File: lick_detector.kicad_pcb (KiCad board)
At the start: 2 copper layers, 74.9 x 80.6 mm, 105 parts, among them P1 PWR_JACK_2.1x5.5_SMD_RA, SW1 SPDT_SLIDE_500A_SM, U1 DRV103, U2 DRV103, U3 DRV103, U4 DRV103, U5 DRV103, U6 DRV103, U7 DRV103, U8 DRV103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

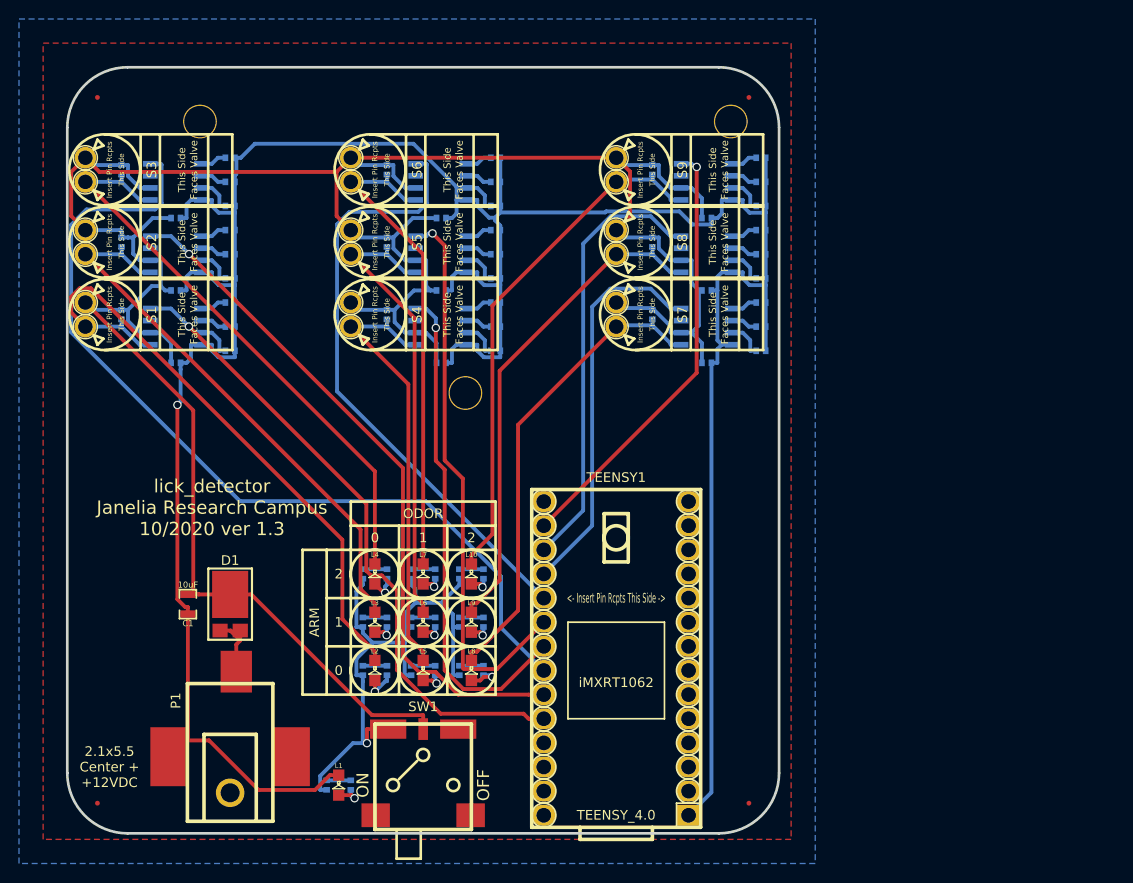
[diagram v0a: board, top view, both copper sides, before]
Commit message: Add ADXL313
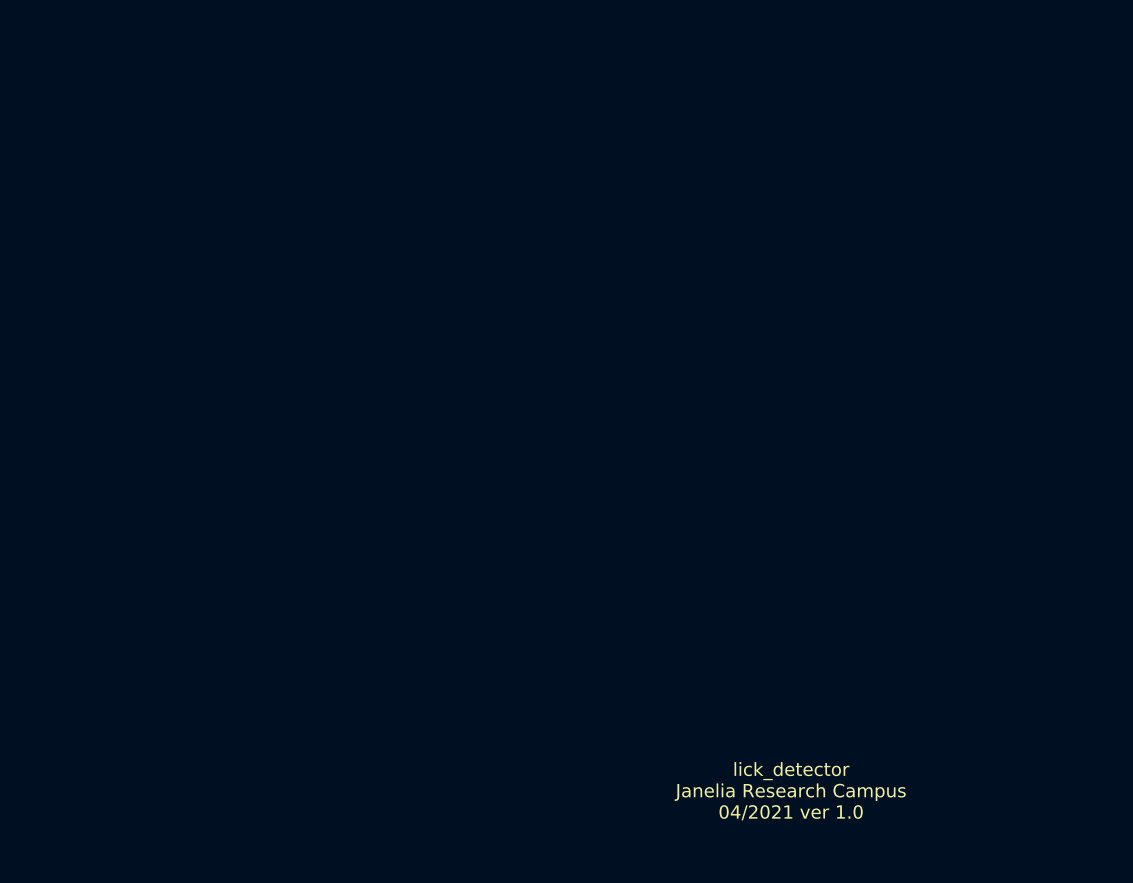
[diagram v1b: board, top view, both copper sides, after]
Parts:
- removed C1: 10uF, lick_detector:SM0805
- removed C10, C12, C14, C16, C18, C2, C4, C6, C8: 1uF, odor_spike_hold:SM0402_POL
- removed C11, C13, C15, C17, C19, C3, C5, C7, C9: 15nF, odor_spike_hold:SM0402
- removed D1: DIODE_SCHOTTKY_45V_10A, lick_detector:CFP15
- removed D10, D12, D14, D16, D18, D20, D4, D6, D8: DIODE_SCHOTTKY_0402, odor_spike_hold:SM0402_POL
- removed D11, D13, D15, D17, D19, D3, D5, D7, D9: DIODE_LOW_REV_CURRENT_0402, odor_spike_hold:SM0402_POL
- removed D2: DIODE_LOW_REV_CURRENT_0402, lick_detector:SM0402_POL
- removed FID1, FID2, FID3, FID4: FIDUCIAL, lick_detector:FIDUCIAL
- removed L1: LED_GRN, lick_detector:LED0805
- removed L10, L2, L3, L4, L5, L6, L7, L8, L9: LED_GRN, odor_spike_hold:LED0805
- removed MH1, MH2, MH3: VAL**, lick_detector:MOUNTING_HOLE_4-40
- removed P1: PWR_JACK_2.1x5.5_SMD_RA, lick_detector:DCJACK_3PAD_SMD_RA
- removed R1: 390, lick_detector:SM0402
- removed R10, R13, R16, R19, R22, R25, R28, R4, R7: 205k, odor_spike_hold:SM0402
- removed R11, R14, R17, R2, R20, R23, R26, R5, R8: 390, odor_spike_hold:SM0402
- removed R12, R15, R18, R21, R24, R27, R3, R6, R9: 150k, odor_spike_hold:SM0402
- removed S1, S2, S3, S4, S5, S6, S7, S8, S9: VAL**, odor_spike_hold:LEECO_LHDB
- removed SW1: SPDT_SLIDE_500A_SM, lick_detector:SPDT_SLIDE_500A_SM
- removed TEENSY1: TEENSY_4.0, lick_detector:TEENSY_4.0
- removed U1, U2, U3, U4, U5, U6, U7, U8, U9: DRV103, odor_spike_hold:SOIC_8
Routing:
- net GND: track 300.6 -> 0.00 mm, vias 1 -> 0
- net VCC: track 286.7 -> 0.00 mm
- net /ARM_0_ODOR_2: track 94.7 -> 0.00 mm
- net /ARM_0_ODOR_1: track 73.0 -> 0.00 mm, vias 1 -> 0
- net /ARM_0_ODOR_0: track 68.3 -> 0.00 mm, vias 1 -> 0
- net /odor_0/SH: track 66.2 -> 0.00 mm
- net /ARM_1_ODOR_2: track 64.0 -> 0.00 mm
- net /Vled: track 63.4 -> 0.00 mm, vias 1 -> 0
- net /odor_2/SH: track 61.2 -> 0.00 mm
- net /ARM_1_ODOR_1: track 59.6 -> 0.00 mm, vias 1 -> 0
- net /odor_1/SH: track 58.7 -> 0.00 mm
- net /odor_8/SH: track 55.0 -> 0.00 mm
- net /ARM_1_ODOR_0: track 53.1 -> 0.00 mm, vias 1 -> 0
- net /odor_7/SH: track 52.7 -> 0.00 mm
- net /odor_5/SH: track 51.8 -> 0.00 mm
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- removed copper zone on B.Cu, net GND
- removed copper zone on F.Cu, net VCC
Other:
- board outline removed
- board text added: "lick_detector Janelia Research Campus 04/2021 ver 1.0"
- board text removed: "0"
- board text removed: "1"
- board text removed: "2"
- board text removed: "2.1x5.5 Center + +12VDC"
- board text removed: "ARM"
- board text removed: "ARM 0"
- board text removed: "ARM 1"
- board text removed: "ARM 2"
- board text removed: "ODOR"
- board text removed: "ODOR 0"
- board text removed: "ODOR 1"
- board text removed: "ODOR 2"
- board text removed: "lick_detector Janelia Research Campus 10/2020 ver 1.3"

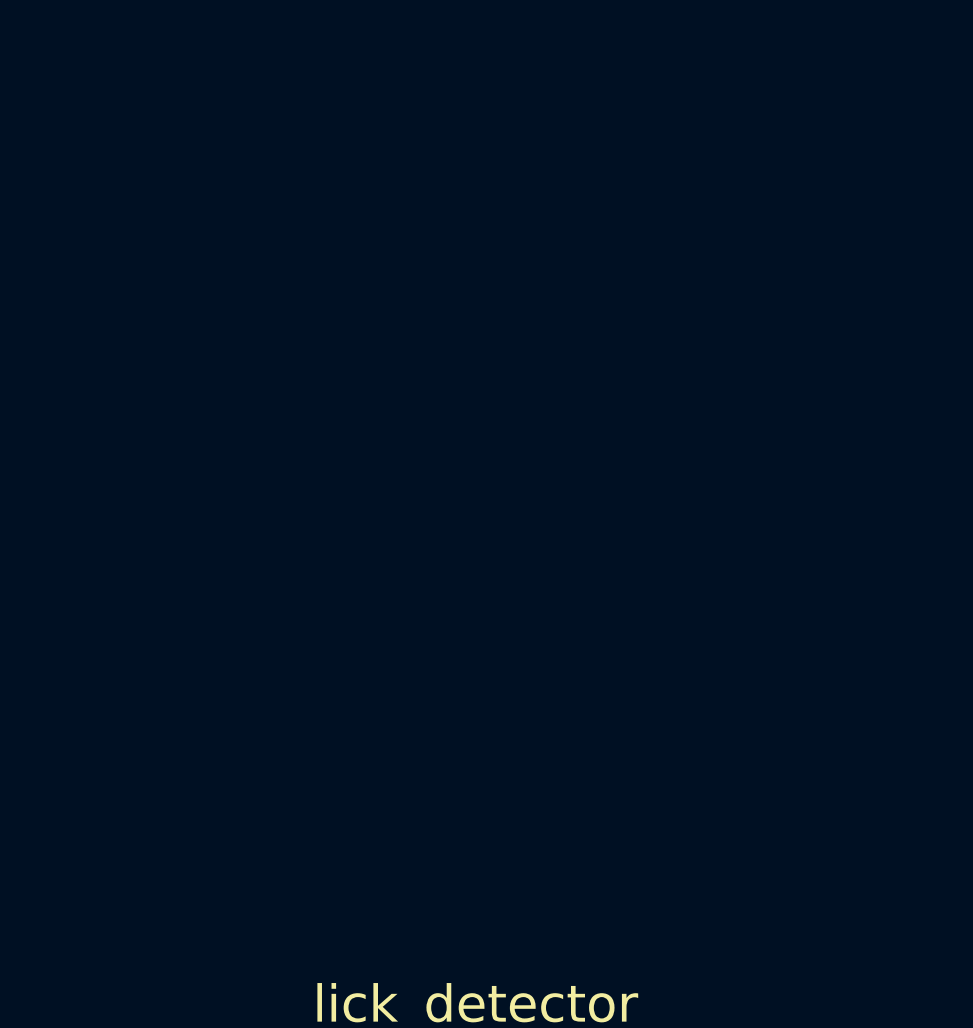
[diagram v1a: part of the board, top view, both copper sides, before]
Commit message: Add capacitors and receptacle
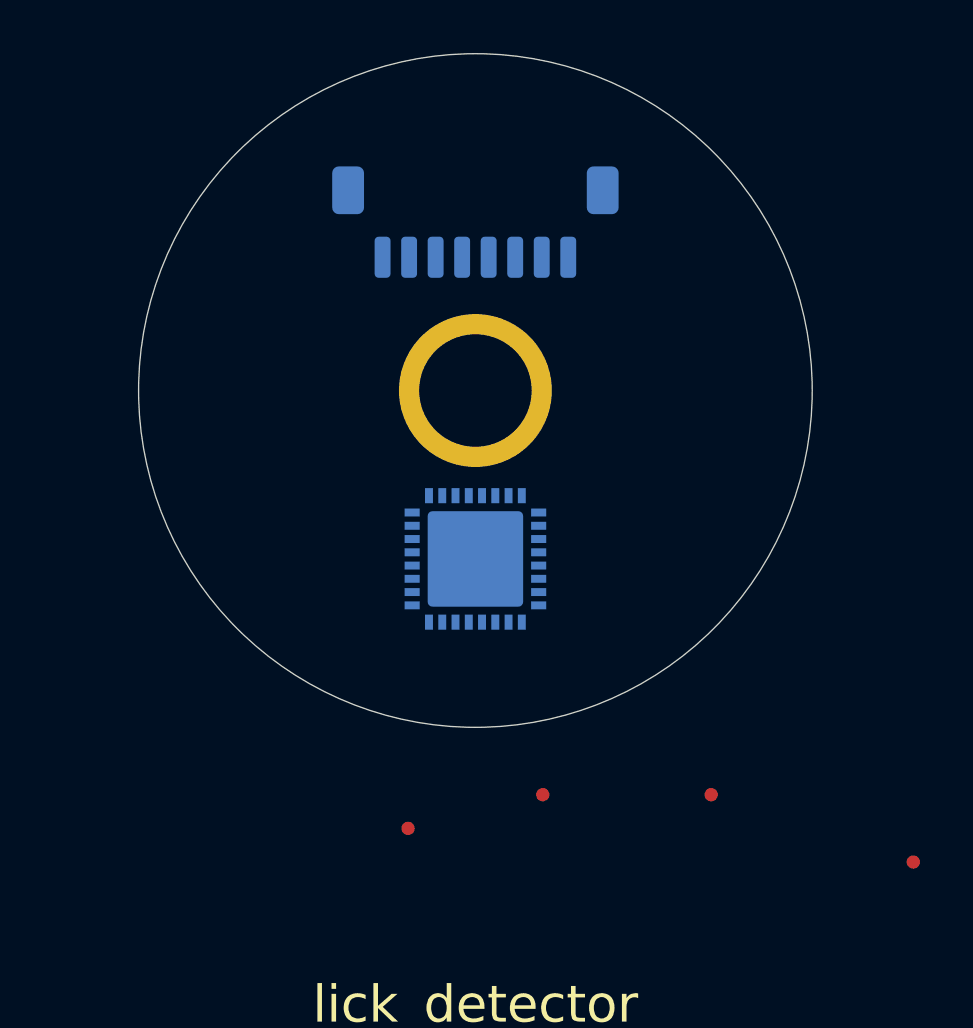
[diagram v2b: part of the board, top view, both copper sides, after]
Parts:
- added FID1: FIDUCIAL, lick_detector:FIDUCIAL, F.Cu at (129.5, 116.8)
- added FID2: FIDUCIAL, lick_detector:FIDUCIAL, F.Cu at (143.5, 119.4)
- added FID3: FIDUCIAL, lick_detector:FIDUCIAL, F.Cu at (135.9, 116.8)
- added FID4: FIDUCIAL, lick_detector:FIDUCIAL, F.Cu at (124.5, 118.1)
- added P1: CONN_PICO_CLASP_8, lick_detector:Molex_Pico-Clasp_501331-0807_1x08-1MP_P1.00mm_Vertical, B.Cu at (127.0, 95.2)
- added P2: RECEPTACLE_2MM, lick_detector:RECEPTACLE_2MM, B.Cu at (127.0, 101.6)
- added U1: ADXL313, lick_detector:LFCSP-32-1EP_5x5mm_P0.5mm_EP3.6x3.6mm, B.Cu at (127.0, 108.0)
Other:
- board outline added: 25.4 x 25.4 mm

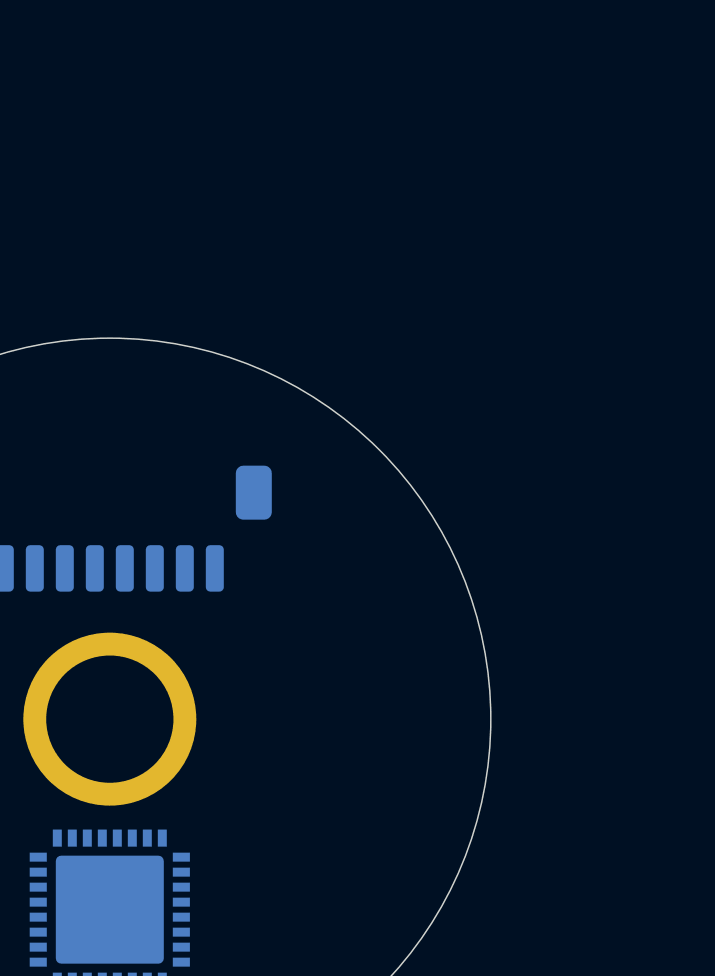
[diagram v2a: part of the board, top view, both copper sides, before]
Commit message: Add BUFFER_TRI_STATE and BUFFER_2_ELEMENT
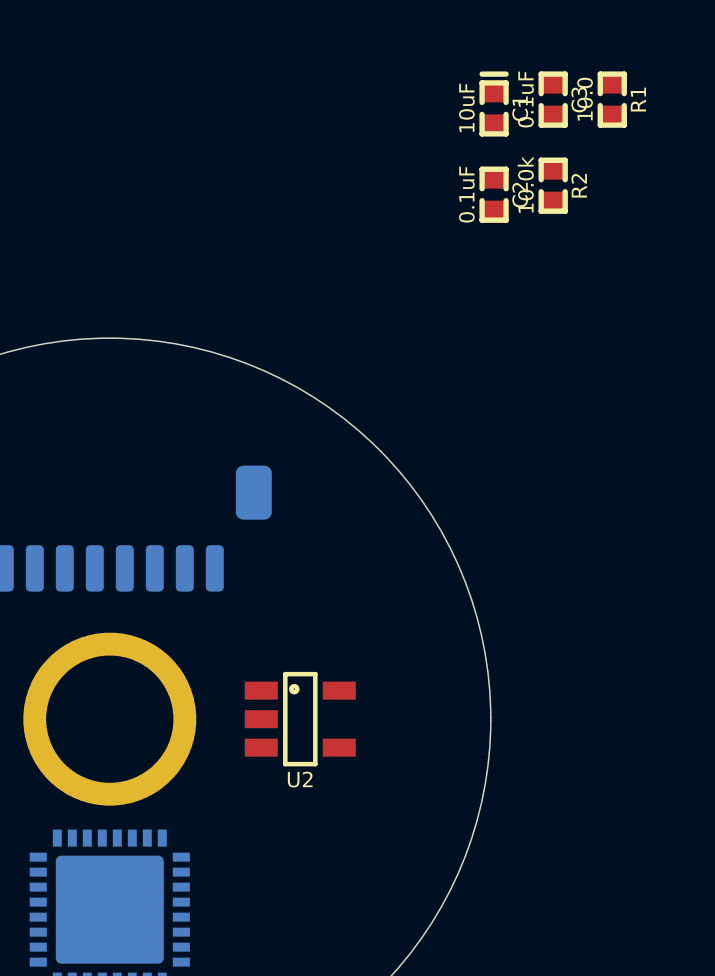
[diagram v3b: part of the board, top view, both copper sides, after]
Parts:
- added C1: 10uF, lick_detector:SM0402_POL, F.Cu at (139.8, 81.2)
- added C2: 0.1uF, lick_detector:SM0402, F.Cu at (139.8, 84.1)
- added C3: 0.1uF, lick_detector:SM0402, F.Cu at (141.8, 80.9)
- added R1: 10.0, lick_detector:SM0402, F.Cu at (143.7, 80.9)
- added R2: 10.0k, lick_detector:SM0402, F.Cu at (141.8, 83.8)
- added U2: BUFFER_TRI_STATE, lick_detector:SOT-23-5, F.Cu at (133.3, 101.6)
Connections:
- P1 pad 1: (no net) -> VAA
- P1 pad 8: (no net) -> GND
- U1 pad 1: (no net) -> GND
- U1 pad 23: (no net) -> /MISO_UB
- U1 pad 3: (no net) -> GND
- U1 pad 33: (no net) -> GND
- U1 pad 4: (no net) -> GND
- U1 pad 5: (no net) -> Net-(R1-Pad1)
- U1 pad 6: (no net) -> /~CS

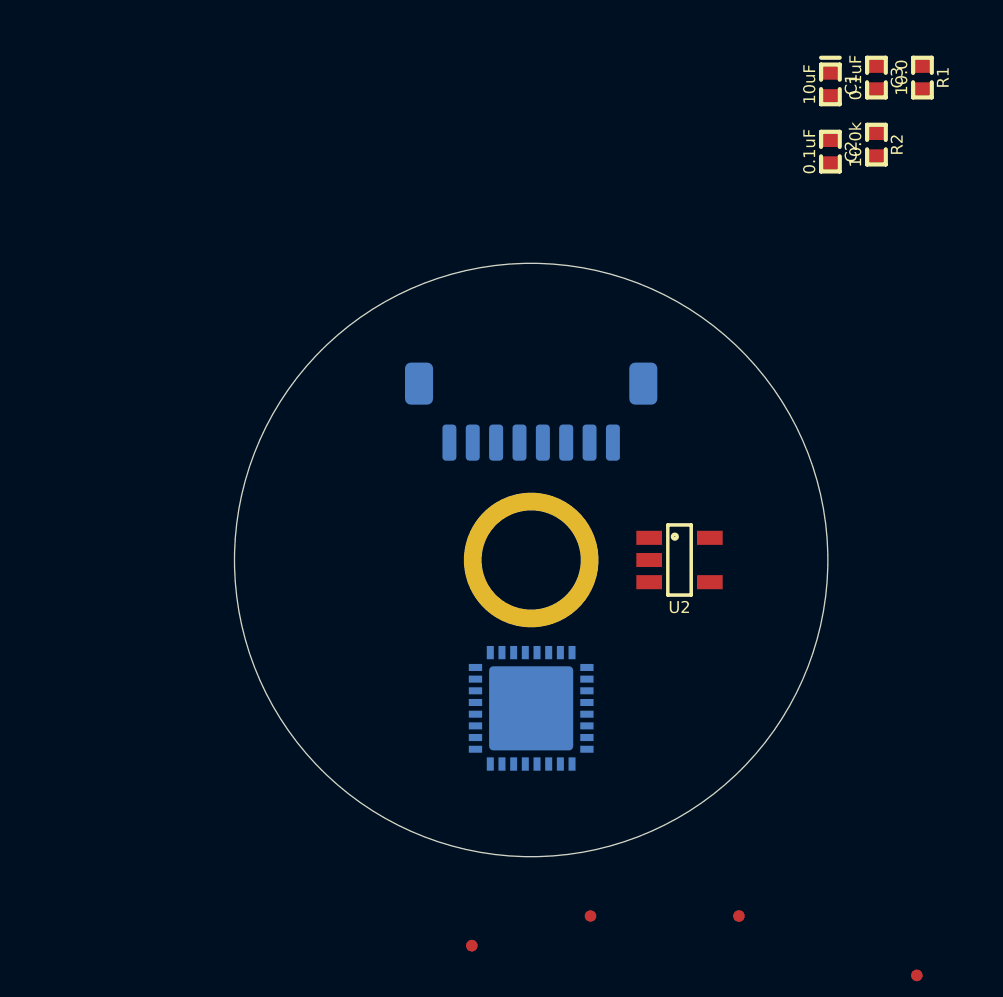
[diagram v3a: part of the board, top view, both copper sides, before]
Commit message: Switch to flex cable
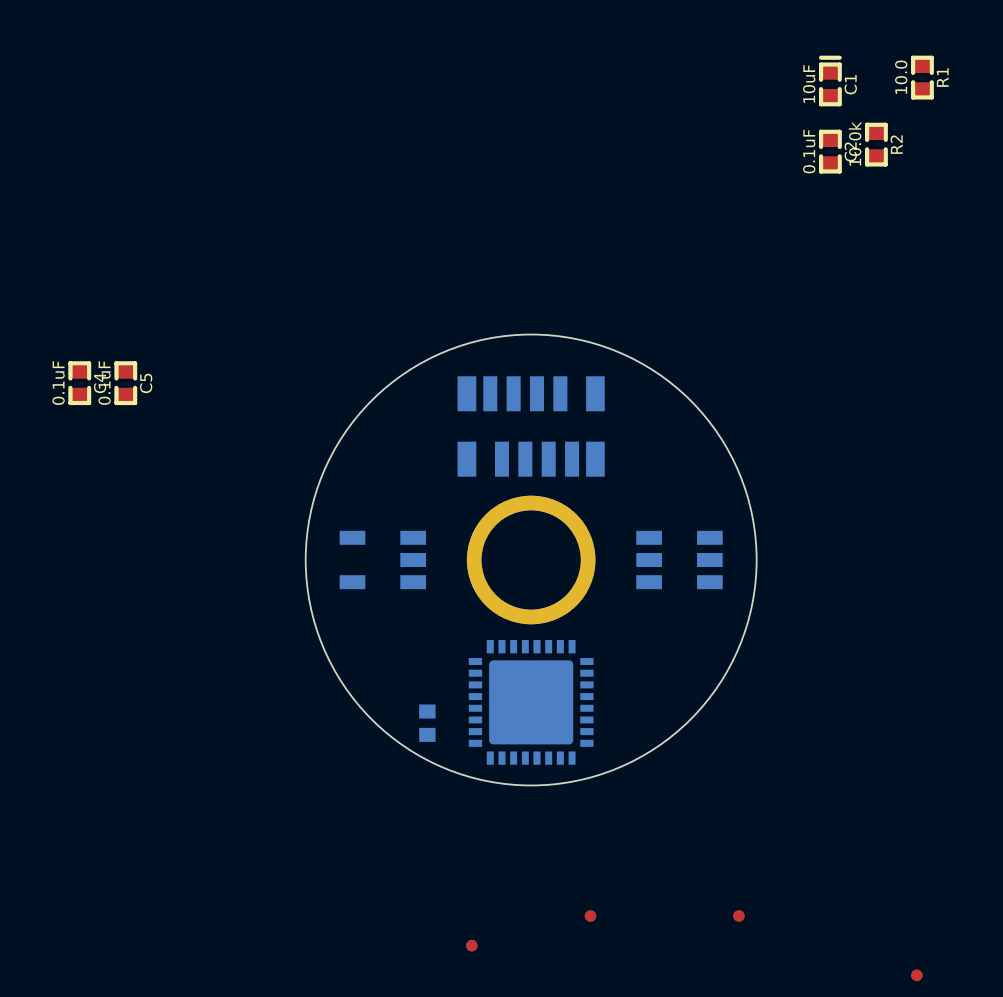
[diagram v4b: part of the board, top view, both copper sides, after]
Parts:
- added C4: 0.1uF, lick_detector:SM0402, F.Cu at (107.7, 94.0)
- added C5: 0.1uF, lick_detector:SM0402, F.Cu at (109.6, 94.0)
- added U3: BUFFER_2_ELEMENT, lick_detector:SOT-23-6, B.Cu at (133.3, 101.6)
- C3, U2: moved to B.Cu
- P1: value CONN_PICO_CLASP_8 -> CONN_FFC_8_VERT; footprint lick_detector:Molex_Pico-Clasp_501331-0807_1x08-1MP_P1.00mm_Vertical -> lick_detector:Molex_FFC_1x8_P0.5mm_Vertical
- moved C3 33.7 mm to (122.6, 108.6)
- moved U2 12.7 mm to (120.7, 101.6), turned to 180 degrees
- moved P1 0.64 mm to (127.0, 95.9)
- moved U1 0.25 mm to (127.0, 107.7)
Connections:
- C1 pad 1: (no net) -> VAA
- C1 pad 2: (no net) -> GND
- C2 pad 1: (no net) -> VAA
- C3 pad 1: (no net) -> VAA
- P1 pad 1: VAA -> GND
- P1 pad 8: GND -> VAA
- R1 pad 2: (no net) -> VAA
- U1 pad 20: (no net) -> /INT1_UB
- U1 pad 21: (no net) -> /INT2_UB
- U1 pad 31: (no net) -> VAA
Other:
- board size 25.4 x 25.4 mm -> 19.3 x 19.3 mm
- net class Default: clearance 0.2 -> 0.1016; trace_width 0.25 -> 0.2032; via_dia 0.8 -> 0.6096; via_drill 0.4 -> 0.3048
- rule pad_to_mask_clearance: 0 -> 0.0508
- rule trace_clearance: 0.2 -> 0.1016

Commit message: Migrate toward 0201
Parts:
- C2, C4, C5: footprint lick_detector:SM0402 -> lick_detector:C_0201_0603Metric
- C3: footprint lick_detector:SM0402 -> lick_detector:C_0201_0603Metric; moved to F.Cu
- P1, P2, U1, U2, U3: moved to F.Cu
- moved R2 34.1 mm to (114.9, 104.8)
- moved R1 30.3 mm to (131.4, 108.6), turned to 90 degrees
- moved C1 24.4 mm to (131.4, 104.1), turned to 90 degrees
- moved C2 24.1 mm to (131.4, 106.7)
- moved C5 24.0 mm to (133.3, 97.8)
- moved U3 23.9 mm to (111.8, 111.8), turned to 0 degrees
- moved C4 13.5 mm to (120.7, 97.8)
- moved U2 11.4 mm to (120.7, 113.0)
- moved U1 0.30 mm to (127.0, 108.0), turned to 180 degrees
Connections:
- U3 pad 2: (no net) -> GND
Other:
- board size 19.3 x 19.3 mm -> 20 x 20 mm
- net class Default: clearance 0.1016 -> 0.0762
- rule trace_clearance: 0.1016 -> 0.0762
